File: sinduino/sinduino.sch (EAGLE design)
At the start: 33 parts, among them IC1 IC_UC_ATMEGA32U4-TQFP44, IC2 TS2940CT5TV, Q1 16000, X1 MINI-USB-32005-301

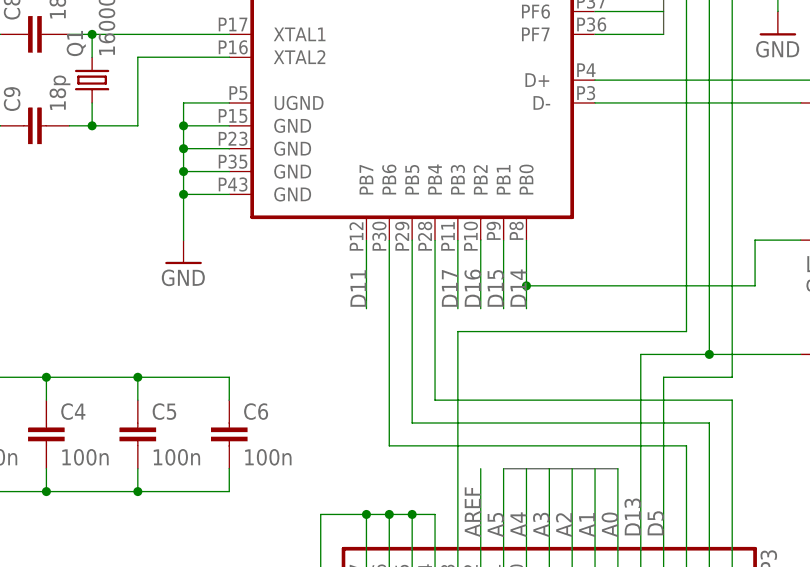
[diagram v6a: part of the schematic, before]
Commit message: name some unnamed signals
and improve xtal routing
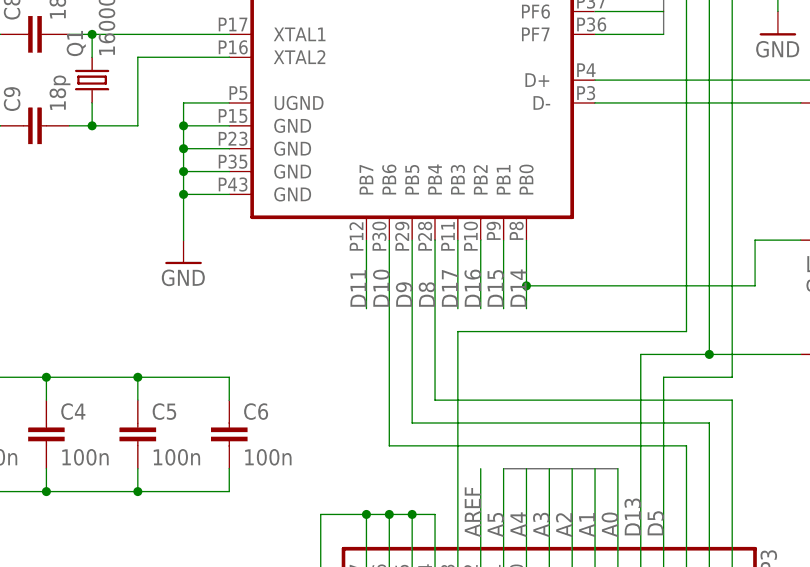
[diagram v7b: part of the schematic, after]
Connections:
- net N$1 renamed D10
- net N$12 renamed D9
- net N$13 renamed D8
- net N$2 renamed TXLED
- net N$3 renamed XTAL1
- net N$4 renamed XTAL2
- net N$6 renamed UCAP
- net N$8 renamed D+
- net N$9 renamed D-
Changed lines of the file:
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@@
 </segment>
 </net>
-<net name="N$3" class="0">
+<net name="XTAL1" class="0">
 <segment>
 <pinref part="C8" gate="G$1" pin="2"/>
@@
 </segment>
 </net>
-<net name="N$4" class="0">
+<net name="XTAL2" class="0">
 <segment>
 <pinref part="IC1" gate="IC" pin="XTAL2"/>
@@
 </segment>
 </net>
-<net name="N$6" class="0">
+<net name="UCAP" class="0">
 <segment>
 <pinref part="IC1" gate="IC" pin="UCAP"/>
@@
 </segment>
 </net>
-<net name="N$8" class="0">
+<net name="D+" class="0">
 <segment>
 <pinref part="R8" gate="G$1" pin="2"/>
@@
 </segment>
 </net>
-<net name="N$9" class="0">
+<net name="D-" class="0">
 <segment>
 <pinref part="IC1" gate="IC" pin="D-"/>
@@
 </segment>
 </net>
-<net name="N$2" class="0">
+<net name="TXLED" class="0">
 <segment>
 <pinref part="IC1" gate="IC" pin="PD5"/>
@@
 </segment>
 </net>
-<net name="N$1" class="0">
+<net name="D10" class="0">
 <segment>
 <pinref part="JP3" gate="G$1" pin="3"/>
@@
 <pinref part="IC1" gate="IC" pin="PB6"/>
 <wire x1="63.5" y1="5.08" x2="63.5" y2="27.94" width="0.1524" layer="91"/>
-</segment>
-</net>
-<net name="N$12" class="0">
+<label x="63.5" y="20.32" size="1.778" layer="95" rot="R90"/>
+</segment>
+</net>
+<net name="D9" class="0">
 <segment>
 <pinref part="IC1" gate="IC" pin="PB5"/>
@@
 <wire x1="66.04" y1="7.62" x2="99.06" y2="7.62" width="0.1524" layer="91"/>
 <wire x1="99.06" y1="7.62" x2="99.06" y2="-10.16" width="0.1524" layer="91"/>
-</segment>
-</net>
-<net name="N$13" class="0">
+<label x="66.04" y="20.32" size="1.778" layer="95" rot="R90"/>
+</segment>
+</net>
+<net name="D8" class="0">
 <segment>
 <pinref part="JP3" gate="G$1" pin="1"/>
@@
 <pinref part="IC1" gate="IC" pin="PB4"/>
 <wire x1="68.58" y1="10.16" x2="68.58" y2="27.94" width="0.1524" layer="91"/>
-</segment>
-</net>
+<label x="68.58" y="20.32" size="1.778" layer="95" rot="R90"/>
+</segment>
+</net>

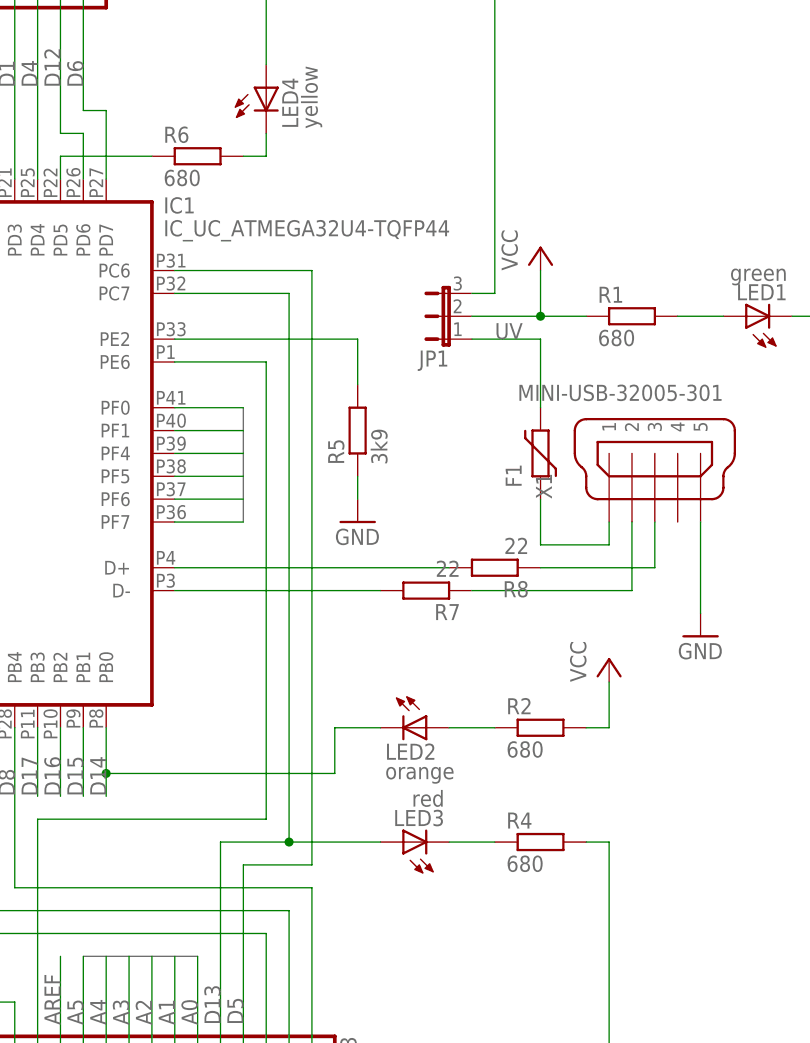
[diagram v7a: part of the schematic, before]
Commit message: adapt resistor values and move one via
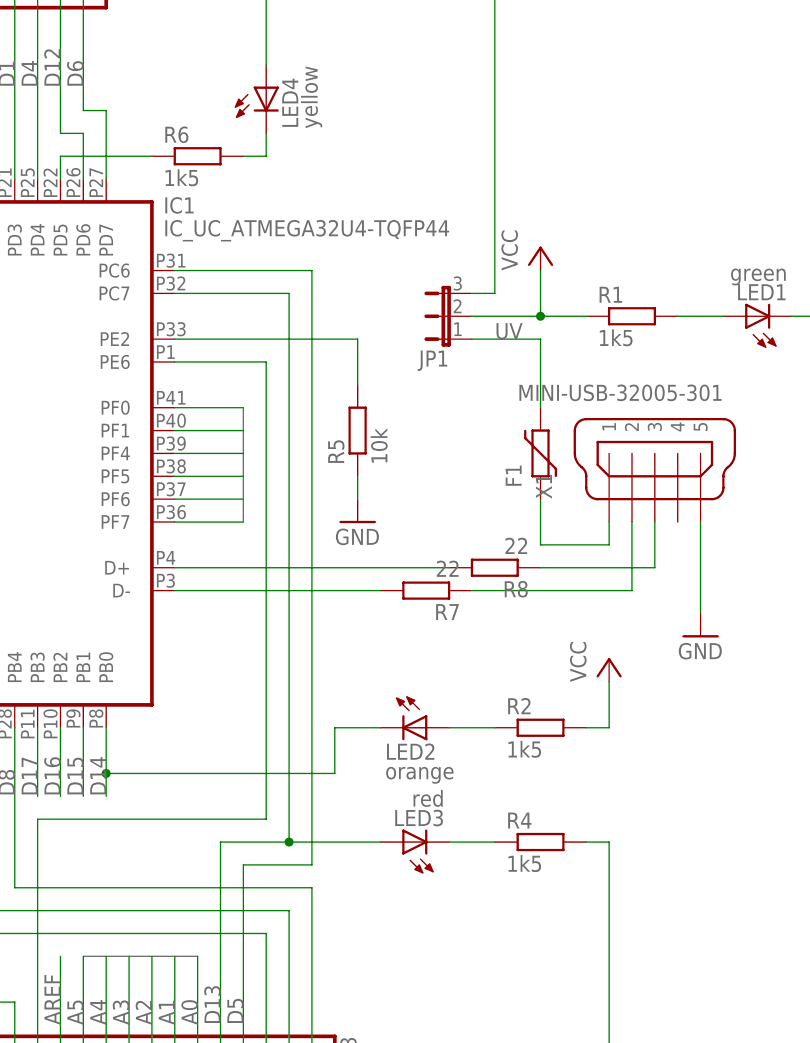
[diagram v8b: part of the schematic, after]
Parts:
- R1, R2, R4, R6: value 680 -> 1k5
- R5: value 3k9 -> 10k
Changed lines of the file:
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@@
 <part name="P+5" library="supply1" deviceset="VCC" device=""/>
 <part name="GND10" library="supply1" deviceset="GND" device=""/>
-<part name="R6" library="rcl" deviceset="R-EU_" device="R1206" value="680"/>
+<part name="R6" library="rcl" deviceset="R-EU_" device="R1206" value="1k5"/>
 <part name="LED4" library="led" deviceset="LED" device="3MM" value="yellow"/>
 <part name="P+1" library="supply1" deviceset="VCC" device=""/>
-<part name="R5" library="rcl" deviceset="R-EU_" device="R1206" value="3k9"/>
+<part name="R5" library="rcl" deviceset="R-EU_" device="R1206" value="10k"/>
 <part name="GND11" library="supply1" deviceset="GND" device=""/>
 <part name="IC2" library="n39" deviceset="TS2940" device="TV" technology="CT5"/>
@@
 <part name="U$3" library="n39" deviceset="RIACON_101_2" device=""/>
 <part name="LED1" library="led" deviceset="LED" device="3MM" value="green"/>
-<part name="R1" library="rcl" deviceset="R-EU_" device="R1206" value="680"/>
+<part name="R1" library="rcl" deviceset="R-EU_" device="R1206" value="1k5"/>
 <part name="GND13" library="supply1" deviceset="GND" device=""/>
-<part name="R2" library="rcl" deviceset="R-EU_" device="R1206" value="680"/>
+<part name="R2" library="rcl" deviceset="R-EU_" device="R1206" value="1k5"/>
 <part name="LED2" library="led" deviceset="LED" device="3MM" value="orange"/>
 <part name="GND14" library="supply1" deviceset="GND" device=""/>
-<part name="R4" library="rcl" deviceset="R-EU_" device="R1206" value="680"/>
+<part name="R4" library="rcl" deviceset="R-EU_" device="R1206" value="1k5"/>
 <part name="LED3" library="led" deviceset="LED" device="3MM" value="red"/>
 <part name="P+3" library="supply1" deviceset="VCC" device=""/>
